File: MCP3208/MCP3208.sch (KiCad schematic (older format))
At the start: 33 parts, among them J1 5V, J2 SPI, J3 CH4, J4 CH3, J5 CH2, J6 CH1, U1 MCP1541, U2 MCP6021, U3 MCP3208

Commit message: Updates to schematic and PCB
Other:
- moved on the sheet: H1, H2, H3, H4
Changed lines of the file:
@@
 L Mechanical:MountingHole H4
 U 1 1 60919793
-P 1600 6050
-F 0 "H4" H 1700 6096 50  0000 L CNN
-F 1 "M3" H 1700 6005 50  0000 L CNN
-F 2 "MountingHole:MountingHole_3.2mm_M3_ISO14580" H 1600 6050 50  0001 C CNN
-F 3 "~" H 1600 6050 50  0001 C CNN
-F 4 "~" H 1600 6050 50  0001 C CNN "Impedence "
-F 5 "~" H 1600 6050 50  0001 C CNN "MPN"
-F 6 "~" H 1600 6050 50  0001 C CNN "Manufacturer"
-F 7 "~" H 1600 6050 50  0001 C CNN "Power"
-F 8 "~" H 1600 6050 50  0001 C CNN "Rating"
-F 9 "~" H 1600 6050 50  0001 C CNN "Tolerance"
-	1    1600 6050
+P 1550 6100
+F 0 "H4" H 1650 6146 50  0000 L CNN
+F 1 "M3" H 1650 6055 50  0000 L CNN
+F 2 "MountingHole:MountingHole_3.2mm_M3_ISO14580" H 1550 6100 50  0001 C CNN
+F 3 "~" H 1550 6100 50  0001 C CNN
+F 4 "~" H 1550 6100 50  0001 C CNN "Impedence "
+F 5 "~" H 1550 6100 50  0001 C CNN "MPN"
+F 6 "~" H 1550 6100 50  0001 C CNN "Manufacturer"
+F 7 "~" H 1550 6100 50  0001 C CNN "Power"
+F 8 "~" H 1550 6100 50  0001 C CNN "Rating"
+F 9 "~" H 1550 6100 50  0001 C CNN "Tolerance"
+	1    1550 6100
 	1    0    0    -1
 $EndComp
@@
 L Mechanical:MountingHole H3
 U 1 1 6091947B
-P 2300 6050
-F 0 "H3" H 2400 6096 50  0000 L CNN
-F 1 "M3" H 2400 6005 50  0000 L CNN
-F 2 "MountingHole:MountingHole_3.2mm_M3_ISO14580" H 2300 6050 50  0001 C CNN
-F 3 "~" H 2300 6050 50  0001 C CNN
-F 4 "~" H 2300 6050 50  0001 C CNN "Impedence "
-F 5 "~" H 2300 6050 50  0001 C CNN "MPN"
-F 6 "~" H 2300 6050 50  0001 C CNN "Manufacturer"
-F 7 "~" H 2300 6050 50  0001 C CNN "Power"
-F 8 "~" H 2300 6050 50  0001 C CNN "Rating"
-F 9 "~" H 2300 6050 50  0001 C CNN "Tolerance"
-	1    2300 6050
+P 2250 6100
+F 0 "H3" H 2350 6146 50  0000 L CNN
+F 1 "M3" H 2350 6055 50  0000 L CNN
+F 2 "MountingHole:MountingHole_3.2mm_M3_ISO14580" H 2250 6100 50  0001 C CNN
+F 3 "~" H 2250 6100 50  0001 C CNN
+F 4 "~" H 2250 6100 50  0001 C CNN "Impedence "
+F 5 "~" H 2250 6100 50  0001 C CNN "MPN"
+F 6 "~" H 2250 6100 50  0001 C CNN "Manufacturer"
+F 7 "~" H 2250 6100 50  0001 C CNN "Power"
+F 8 "~" H 2250 6100 50  0001 C CNN "Rating"
+F 9 "~" H 2250 6100 50  0001 C CNN "Tolerance"
+	1    2250 6100
 	1    0    0    -1
 $EndComp
@@
 L Mechanical:MountingHole H2
 U 1 1 60919211
-P 2300 5700
-F 0 "H2" H 2400 5746 50  0000 L CNN
-F 1 "M3" H 2400 5655 50  0000 L CNN
-F 2 "MountingHole:MountingHole_3.2mm_M3_ISO14580" H 2300 5700 50  0001 C CNN
-F 3 "~" H 2300 5700 50  0001 C CNN
-F 4 "~" H 2300 5700 50  0001 C CNN "Impedence "
-F 5 "~" H 2300 5700 50  0001 C CNN "MPN"
-F 6 "~" H 2300 5700 50  0001 C CNN "Manufacturer"
-F 7 "~" H 2300 5700 50  0001 C CNN "Power"
-F 8 "~" H 2300 5700 50  0001 C CNN "Rating"
-F 9 "~" H 2300 5700 50  0001 C CNN "Tolerance"
-	1    2300 5700
+P 2250 5750
+F 0 "H2" H 2350 5796 50  0000 L CNN
+F 1 "M3" H 2350 5705 50  0000 L CNN
+F 2 "MountingHole:MountingHole_3.2mm_M3_ISO14580" H 2250 5750 50  0001 C CNN
+F 3 "~" H 2250 5750 50  0001 C CNN
+F 4 "~" H 2250 5750 50  0001 C CNN "Impedence "
+F 5 "~" H 2250 5750 50  0001 C CNN "MPN"
+F 6 "~" H 2250 5750 50  0001 C CNN "Manufacturer"
+F 7 "~" H 2250 5750 50  0001 C CNN "Power"
+F 8 "~" H 2250 5750 50  0001 C CNN "Rating"
+F 9 "~" H 2250 5750 50  0001 C CNN "Tolerance"
+	1    2250 5750
 	1    0    0    -1
 $EndComp
@@
 L Mechanical:MountingHole H1
 U 1 1 60918BE5
-P 1600 5700
-F 0 "H1" H 1700 5746 50  0000 L CNN
-F 1 "M3" H 1700 5655 50  0000 L CNN
-F 2 "MountingHole:MountingHole_3.2mm_M3_ISO14580" H 1600 5700 50  0001 C CNN
-F 3 "~" H 1600 5700 50  0001 C CNN
-F 4 "~" H 1600 5700 50  0001 C CNN "Impedence "
-F 5 "~" H 1600 5700 50  0001 C CNN "MPN"
-F 6 "~" H 1600 5700 50  0001 C CNN "Manufacturer"
-F 7 "~" H 1600 5700 50  0001 C CNN "Power"
-F 8 "~" H 1600 5700 50  0001 C CNN "Rating"
-F 9 "~" H 1600 5700 50  0001 C CNN "Tolerance"
-	1    1600 5700
+P 1550 5750
+F 0 "H1" H 1650 5796 50  0000 L CNN
+F 1 "M3" H 1650 5705 50  0000 L CNN
+F 2 "MountingHole:MountingHole_3.2mm_M3_ISO14580" H 1550 5750 50  0001 C CNN
+F 3 "~" H 1550 5750 50  0001 C CNN
+F 4 "~" H 1550 5750 50  0001 C CNN "Impedence "
+F 5 "~" H 1550 5750 50  0001 C CNN "MPN"
+F 6 "~" H 1550 5750 50  0001 C CNN "Manufacturer"
+F 7 "~" H 1550 5750 50  0001 C CNN "Power"
+F 8 "~" H 1550 5750 50  0001 C CNN "Rating"
+F 9 "~" H 1550 5750 50  0001 C CNN "Tolerance"
+	1    1550 5750
 	1    0    0    -1
 $EndComp
-Text Notes 1400 5450 0    79   ~ 0
+Text Notes 1350 5500 0    79   ~ 0
 Mounting Holes
 Wire Notes Line
-	1300 5250 2700 5250
+	1250 5300 2650 5300
 Wire Notes Line
-	2700 5250 2700 6300
+	2650 5300 2650 6350
 Wire Notes Line
-	2700 6300 1300 6300
+	2650 6350 1250 6350
 Wire Notes Line
-	1300 6300 1300 5250
+	1250 6350 1250 5300
 Connection ~ 3900 1500
 Wire Wire Line

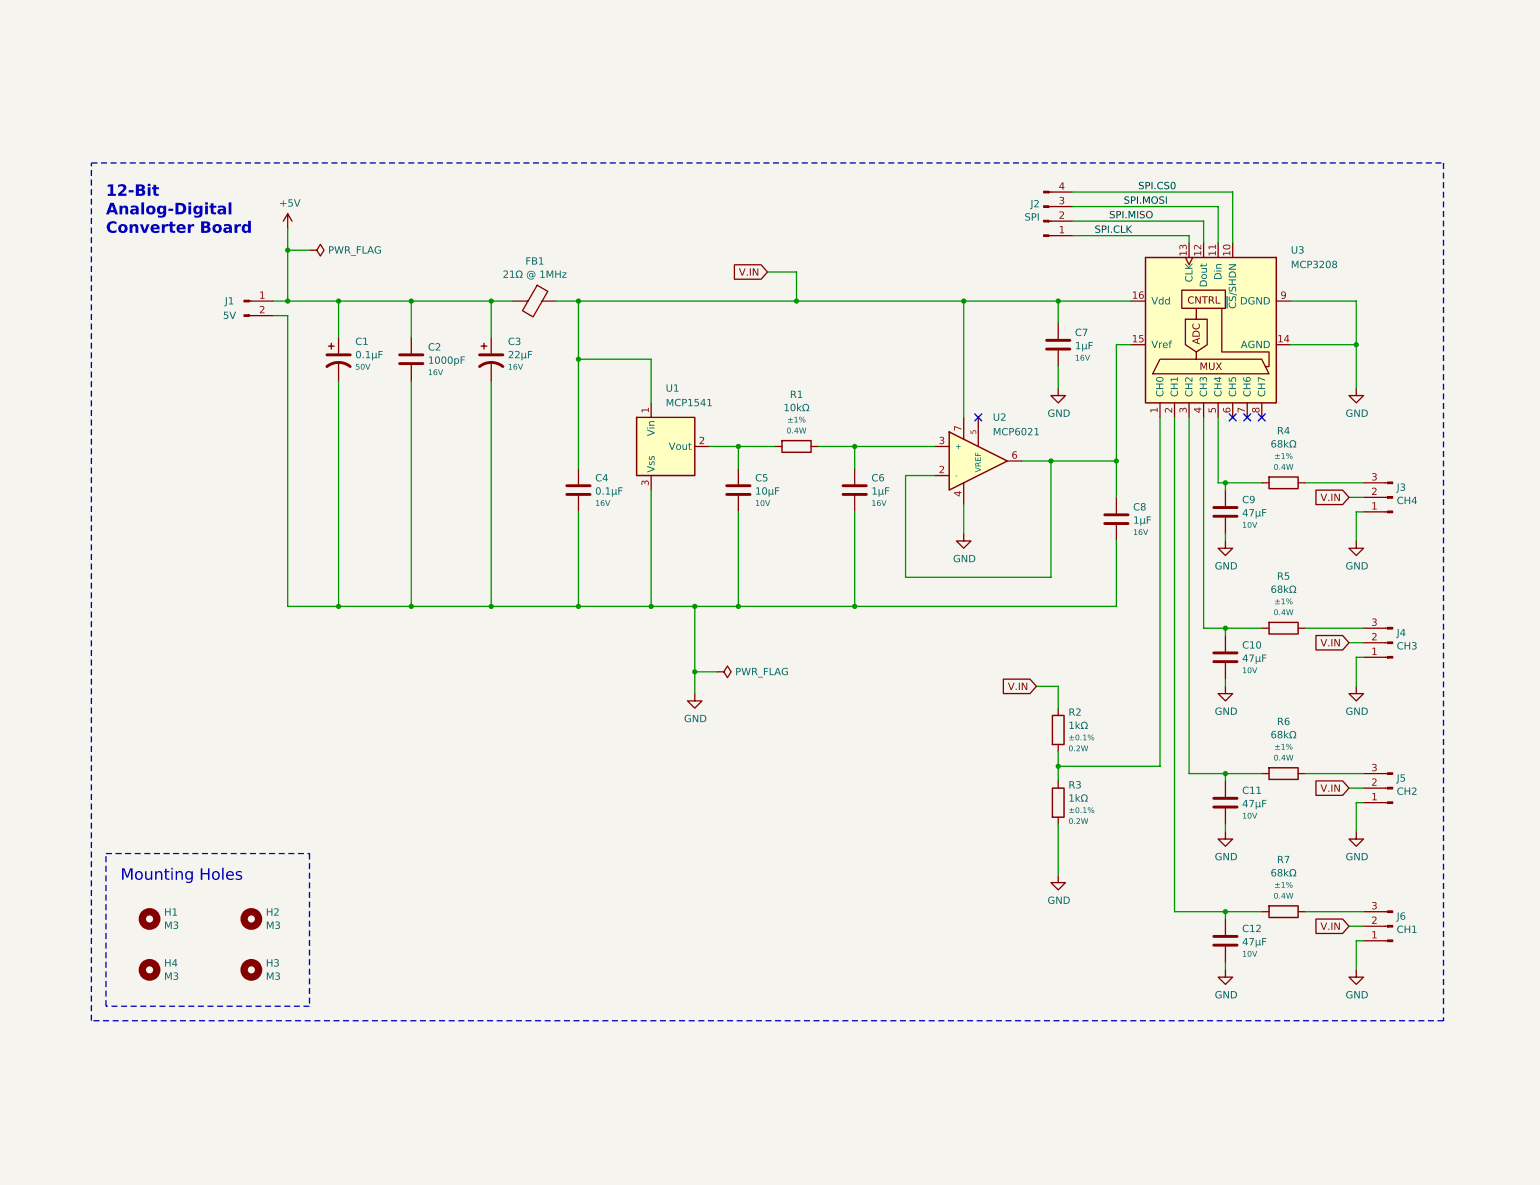
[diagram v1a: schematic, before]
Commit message: Changes to schematic layout
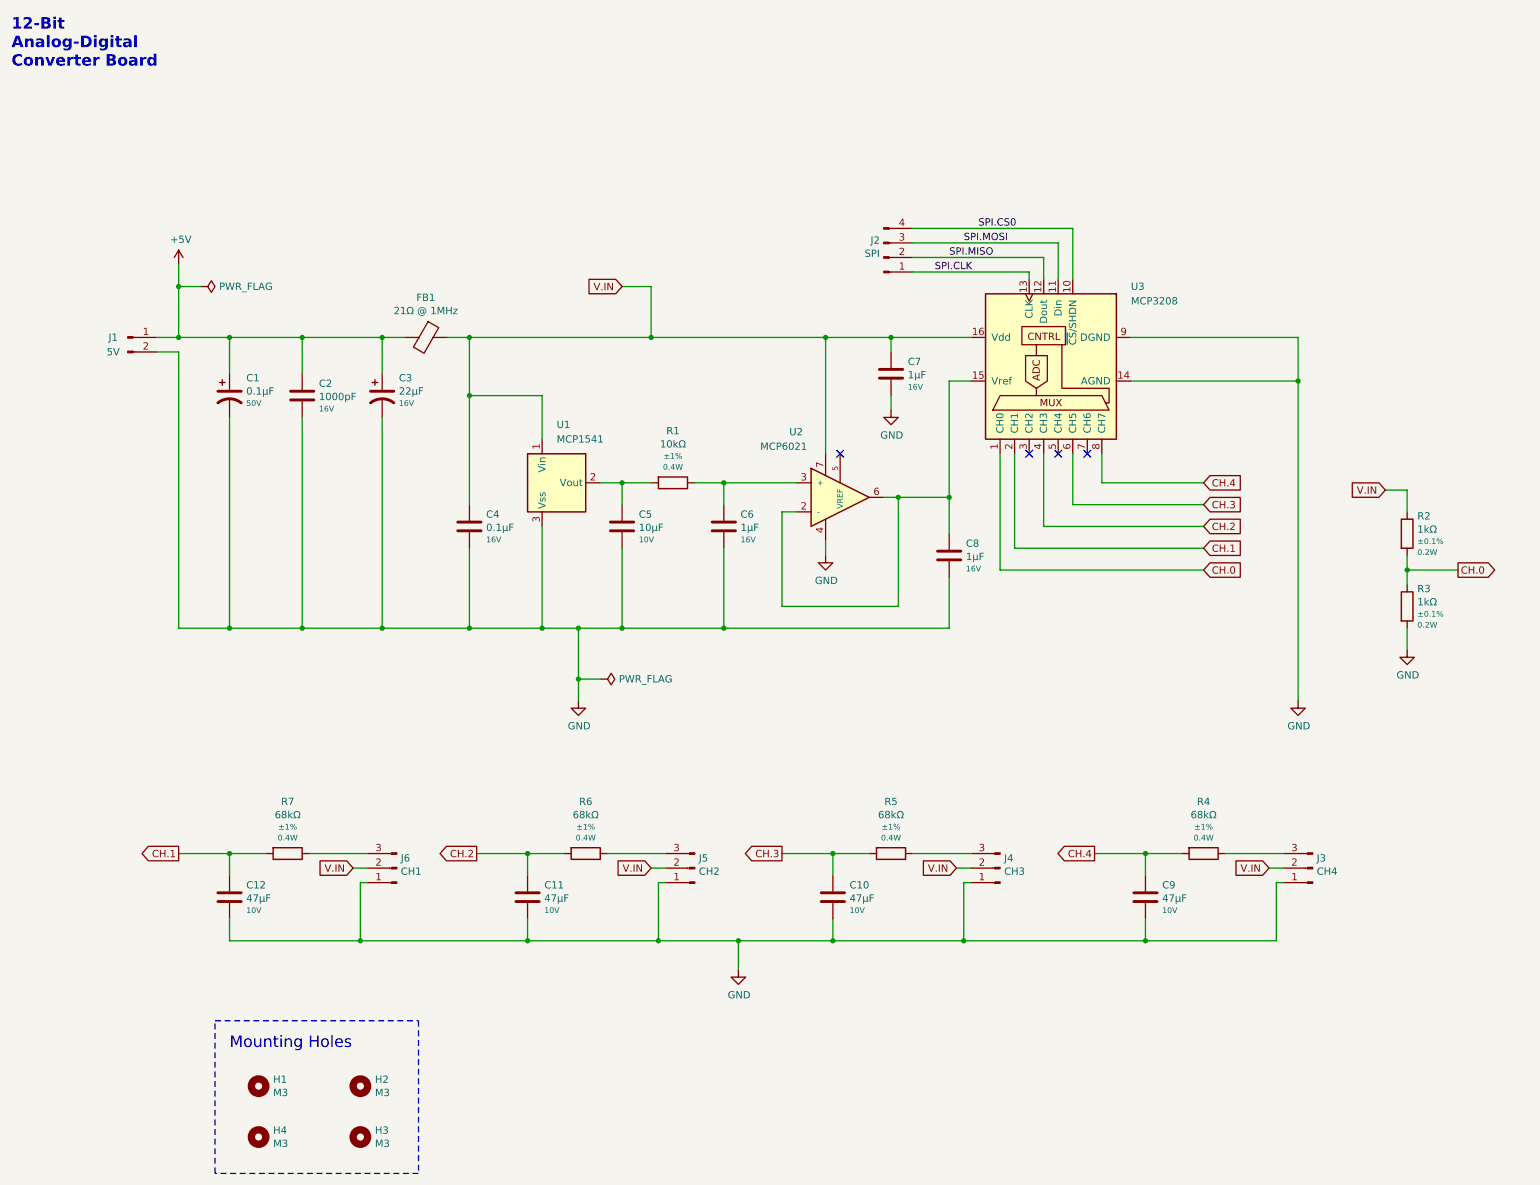
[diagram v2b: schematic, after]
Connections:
- net CH.0: now reaches R2.2, R3.1, U3.1 (CH0)
- net CH.1: now reaches C12.2, R7.2, U3.2 (CH1)
- net CH.2: now reaches C11.2, R6.2
- net CH.2: now also U3.4 (CH3); no longer U3.3 (CH2)
- net CH.3: now reaches C10.2, R5.2
- net CH.3: now also U3.6 (CH5); no longer U3.4 (CH3)
- net CH.4: now reaches C9.2, R4.2
- net CH.4: now also U3.8 (CH7); no longer U3.5 (CH4)
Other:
- moved on the sheet: C1, C10, C11, C12, C2, C3, C4, C5, C6, C7, C8, C9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

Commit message: Changes to footprints
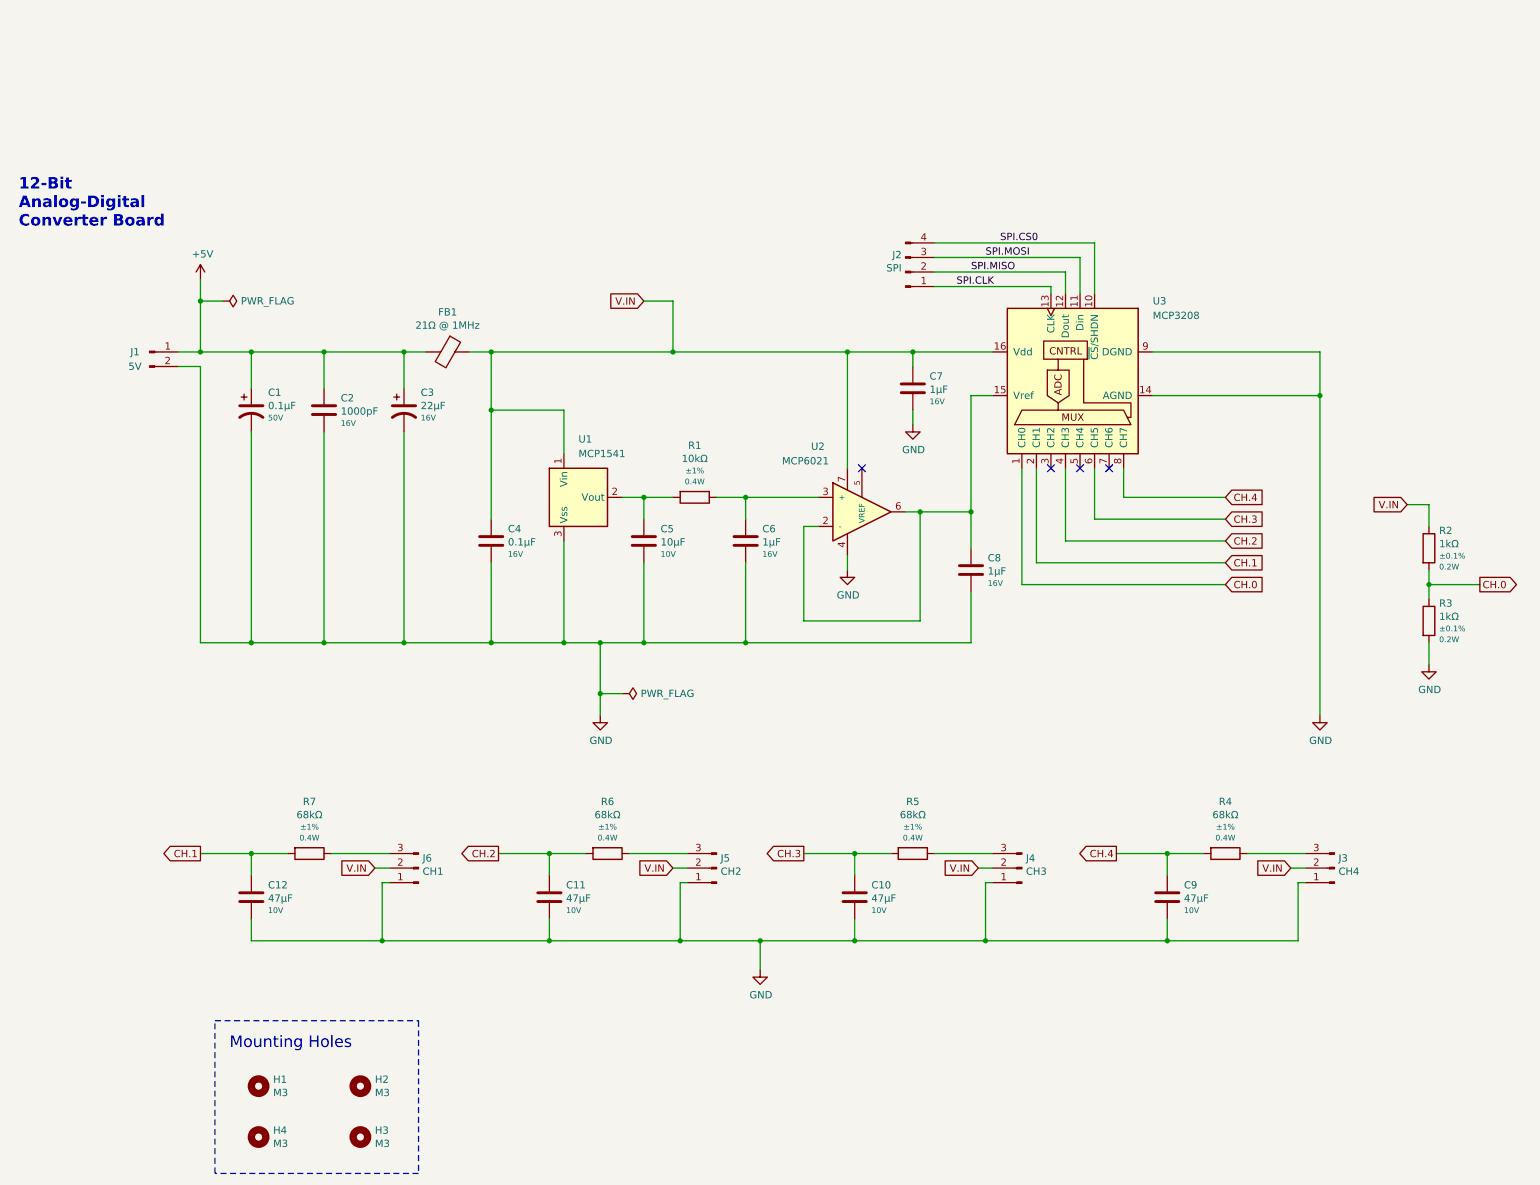
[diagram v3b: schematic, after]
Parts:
- C1: footprint Capacitor_SMD:CP_Elec_4x4.5 -> Capacitor_SMD:CP_Elec_4x4.5_HandSolder
- C3: footprint Capacitor_SMD:CP_Elec_5x5.3 -> Capacitor_SMD:CP_Elec_5x5.3_HandSolder
- FB1: footprint Ferrite_THT:FIL_NFZ32BW210HN11L -> Ferrite_THT:FIL_NFZ32BW210HN11L_HandSolder
- U1: footprint Package_TO_SOT_SMD:SOT-23 -> Package_TO_SOT_SMD:SOT-23_Handsoldering_MCP
- U2: footprint Package_SO:SOIC-8_3.9x4.9mm_P1.27mm -> Package_SO:SOIC-8_MCP_HandSolder
- U3: footprint Package_SO:SOIC-16_3.9x9.9mm_P1.27mm -> Package_SO:SOIC-16_MCP_HandSolder
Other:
- moved on the sheet: C1, C10, C11, C12, C2, C3, C4, C5, C6, C7, C8, C9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
